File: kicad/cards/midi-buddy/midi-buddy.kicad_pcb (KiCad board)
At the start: 2 copper layers, 38 x 64 mm, 31 parts, among them J1 Conn_01x06_Pin, J2 Conn_01x06_Pin, J3 MIDI_IN, J4 Conn_01x05, J5 MIDI_OUT, Q1 MMBT3904, U1 THVD1450DR, U2 STM32C011F4Px, U6 TLP291

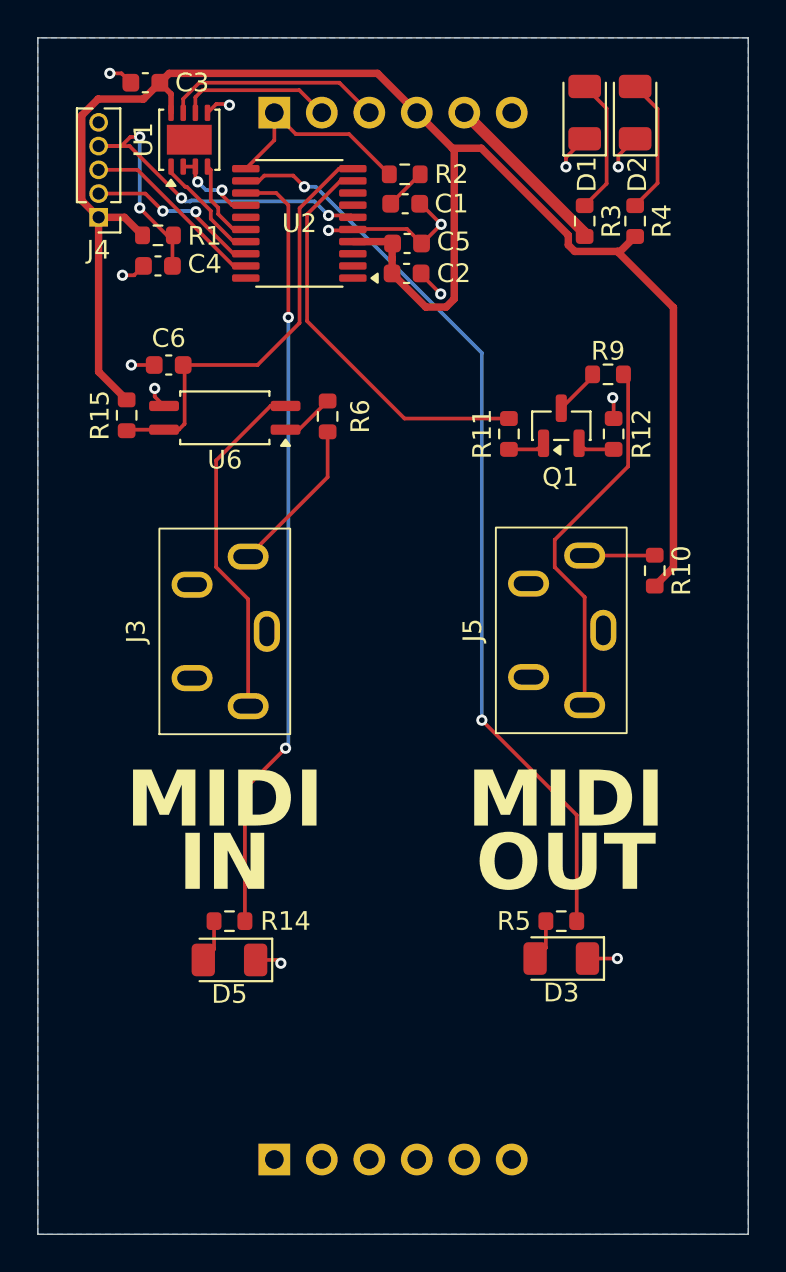
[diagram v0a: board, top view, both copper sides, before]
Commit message: Update card template and MIDI Buddy
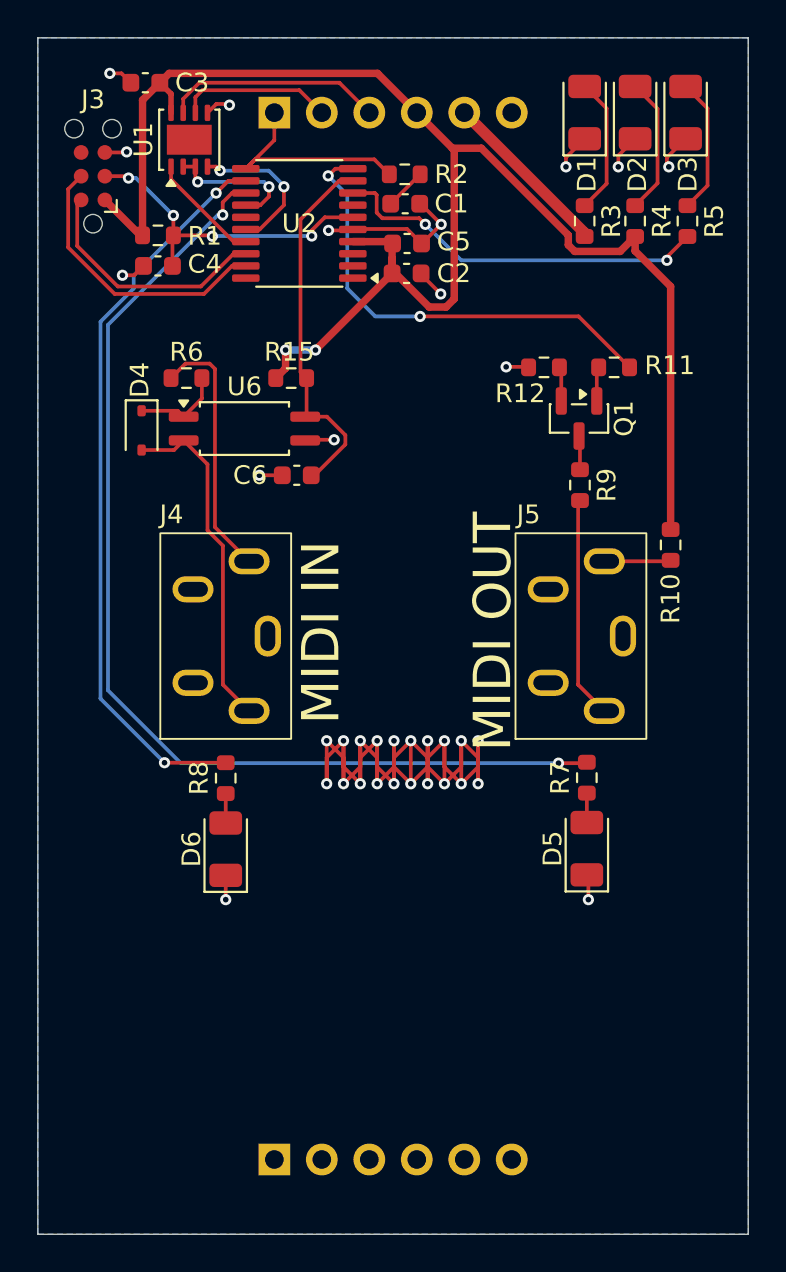
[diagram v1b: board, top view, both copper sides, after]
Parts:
- removed R14: 1K, Resistor_SMD:R_0603_1608Metric
- added D4: 1N914, Diode_SMD:D_SOD-323, F.Cu at (127.8, 74.5)
- added D6: LED, LED_SMD:LED_1206_3216Metric, F.Cu at (132.3, 96.9)
- added R7: 1K, Resistor_SMD:R_0603_1608Metric, F.Cu at (151.6, 93.1)
- added R8: 1K, Resistor_SMD:R_0603_1608Metric, F.Cu at (132.3, 93.1)
- J3: value MIDI_IN -> Conn_ARM_SWD_TagConnect_TC2030-NL; footprint BuddySystem:PJ-358 -> Connector:Tag-Connect_TC2030-IDC-NL_2x03_P1.27mm_Vertical
- J4: value Conn_01x05 -> MIDI_IN; footprint Connector_PinHeader_1.27mm:PinHeader_1x05_P1.27mm_Vertical -> BuddySystem:PJ-358
- moved D3 45.7 mm to (156.9, 57.5), turned to 90 degrees
- moved R5 38.1 mm to (157.0, 63.3), turned to -90 degrees
- moved J3 25.2 mm to (125.2, 60.9)
- moved J4 23.3 mm to (131.8, 85.5), turned to 90 degrees
- moved D5 20.0 mm to (151.6, 96.9), turned to 90 degrees
- moved C6 9.04 mm to (136.1, 76.9)
- moved R15 9.02 mm to (135.8, 71.7), turned to 180 degrees
- moved R6 7.82 mm to (130.2, 71.7), turned to 0 degrees
- moved R11 6.66 mm to (153.1, 71.1), turned to 0 degrees
- moved R9 6.11 mm to (151.2, 77.4), turned to -90 degrees
- moved R12 5.15 mm to (149.3, 71.1), turned to 180 degrees
- moved R10 1.62 mm to (156.1, 80.6), turned to 90 degrees
- moved U6 1.20 mm to (133.3, 74.4), turned to 0 degrees
- moved J5 1.09 mm to (150.8, 85.5)
- moved Q1 1.03 mm to (151.2, 73.9), turned to -90 degrees
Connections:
- J1 pad 1: unconnected-(J1-Pin_1-Pad1) -> MCLK
- J1 pad 2: unconnected-(J1-Pin_2-Pad2) -> BLCK
- J1 pad 3: unconnected-(J1-Pin_3-Pad3) -> FSYNC
- J1 pad 4: unconnected-(J1-Pin_4-Pad4) -> S4_AUDIO_IN
- J1 pad 5: unconnected-(J1-Pin_5-Pad5) -> S4_AUDIO_OUT
- R5 pad 2: MIDI_OUT_ACT -> ACC
- R6 pad 1: Net-(J3-PadR) -> Net-(J4-PadR)
- U2 pad 10: MIDI_IN_UART -> MIDI_OUT_UART
- U2 pad 12: MIDI_OUT_ACT -> MIDI_IN_ACT
- U2 pad 13: MIDI_IN_ACT -> MIDI_OUT_ACT
- U2 pad 8: unconnected-(U2-PA1-Pad8) -> ACC
- U2 pad 9: MIDI_OUT_UART -> MIDI_IN_UART
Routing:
- net GND: track 24.3 -> 94.5 mm, vias 13 -> 35
- net ACC: track 0.00 -> 20.6 mm, vias 0 -> 2
- net Net-(J4-PadR): track 0.00 -> 13.8 mm
- net Net-(J3-PadR): track 8.44 -> 0.00 mm
- net MIDI_OUT_ACT: track 49.2 -> 57.5 mm
- net Net-(J5-PadT): track 20.1 -> 11.9 mm
- net NRST: track 25.5 -> 17.5 mm
- net +3V3: track 91.6 -> 85.8 mm, vias 0 -> 2
- net SWCLK: track 10.0 -> 15.3 mm
- net Net-(D3-A): track 2.24 -> 7.31 mm
- net SWDIO: track 9.34 -> 13.2 mm, vias 2 -> 0
- net BUS_TX: track 4.60 -> 8.12 mm, vias 0 -> 2
- net MIDI_IN_UART: track 23.5 -> 19.9 mm
- net MIDI_OUT_UART: track 21.9 -> 24.8 mm, vias 0 -> 2
- net BUS_EN: track 4.77 -> 7.39 mm
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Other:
- board text added: "MIDI IN"
- board text added: "MIDI OUT"
- board text removed: "IN"
- board text removed: "OUT"
